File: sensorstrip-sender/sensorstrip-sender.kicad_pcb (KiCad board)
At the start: 2 copper layers, 56 x 13 mm, 14 parts, among them J1 USB_C_Receptacle_PowerOnly, J2 Conn_01x02_MountingPin, SW1 SW_DPDT_x2

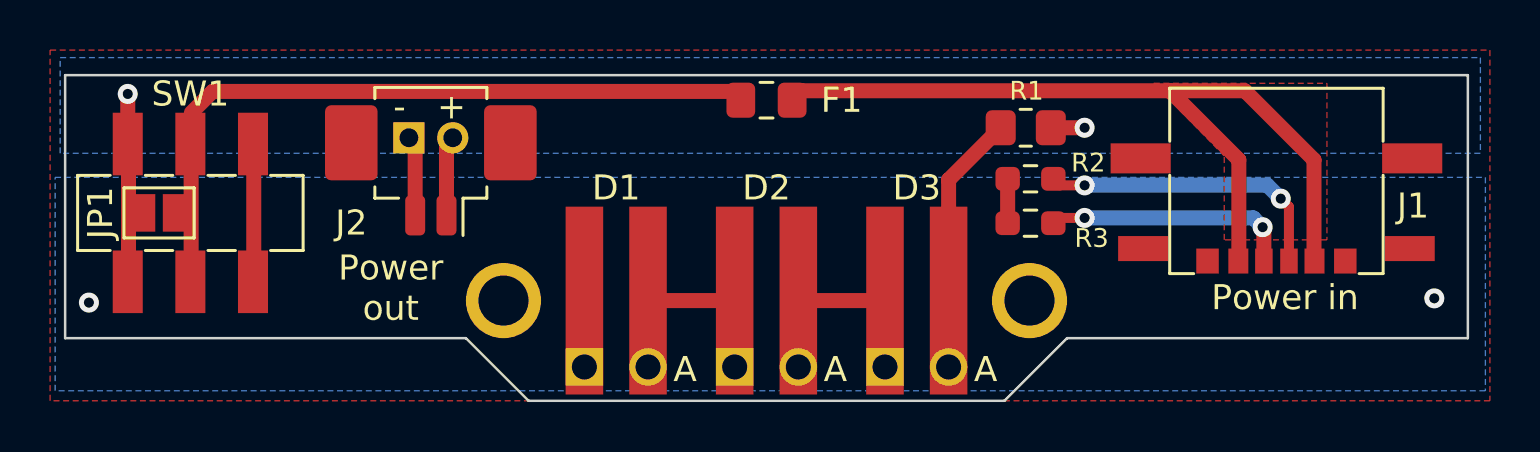
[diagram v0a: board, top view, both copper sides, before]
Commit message: Minor sensorstrip-sender revision:
- Swap PTH for NPTH
- Add through-holes to power switch pads for switch relocation
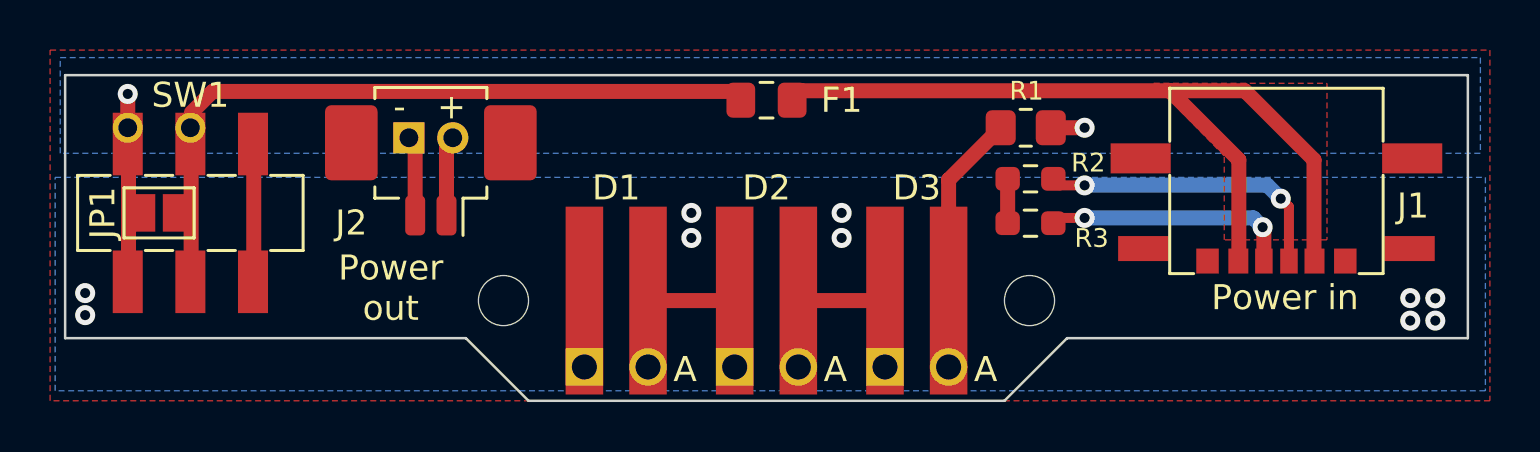
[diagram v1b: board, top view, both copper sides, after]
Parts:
- ? (x2): value MountingHole-2mm-PTH -> MountingHole-2mm-NPTH; footprint sensorstrip:MountingHole-2mm-PTH -> sensorstrip:MountingHole-2mm-NPTH
- SW1: footprint sensorstrip:JS202011SCQN -> sensorstrip:JS202011SCQN-Hybrid
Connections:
- ? pad : GND -> (no net) (x2)
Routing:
- net GND: vias 2 -> 10
